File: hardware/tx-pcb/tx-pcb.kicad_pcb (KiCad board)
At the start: 4 copper layers, 70 x 79.1 mm, 61 parts, among them J1 Conn_To_J1, J2 Conn_To_J2, J3 BLIO, J4 Conn_01x05, J5 Conn_01x04, J6 PWRO, J7 Conn_01x02_Pin, SW1 BOOT0, SW2 RESET, SW3 BTN1, SW4 BTN2, SW5 BTN3, SW6 BTN4, SW7 BTN5, SW9 SW_SPDT, U2 STM32WB55CEUx, X1 Q22FA12800025, X2 ABS07-32.768KHZ-1-T

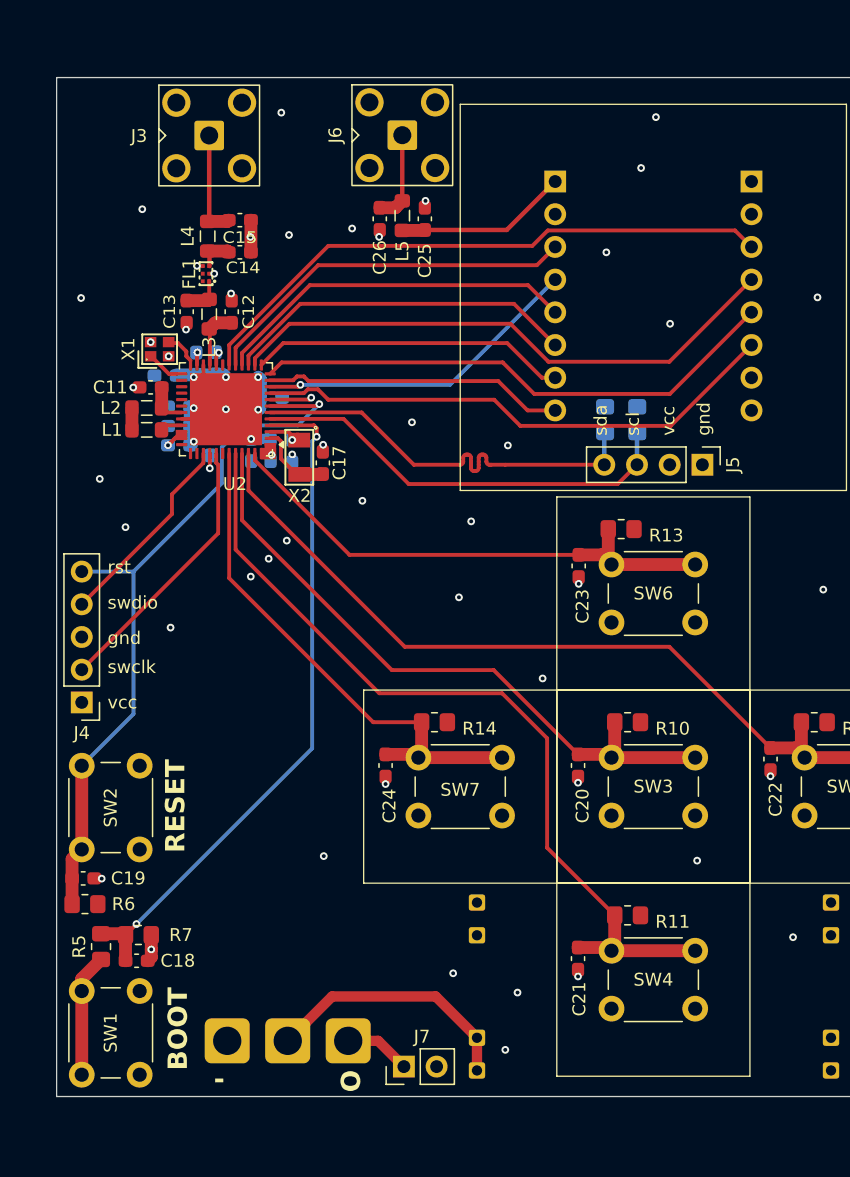
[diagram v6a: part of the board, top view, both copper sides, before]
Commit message: updated bluetooth output for MLPF chip and fixed ground layer issue
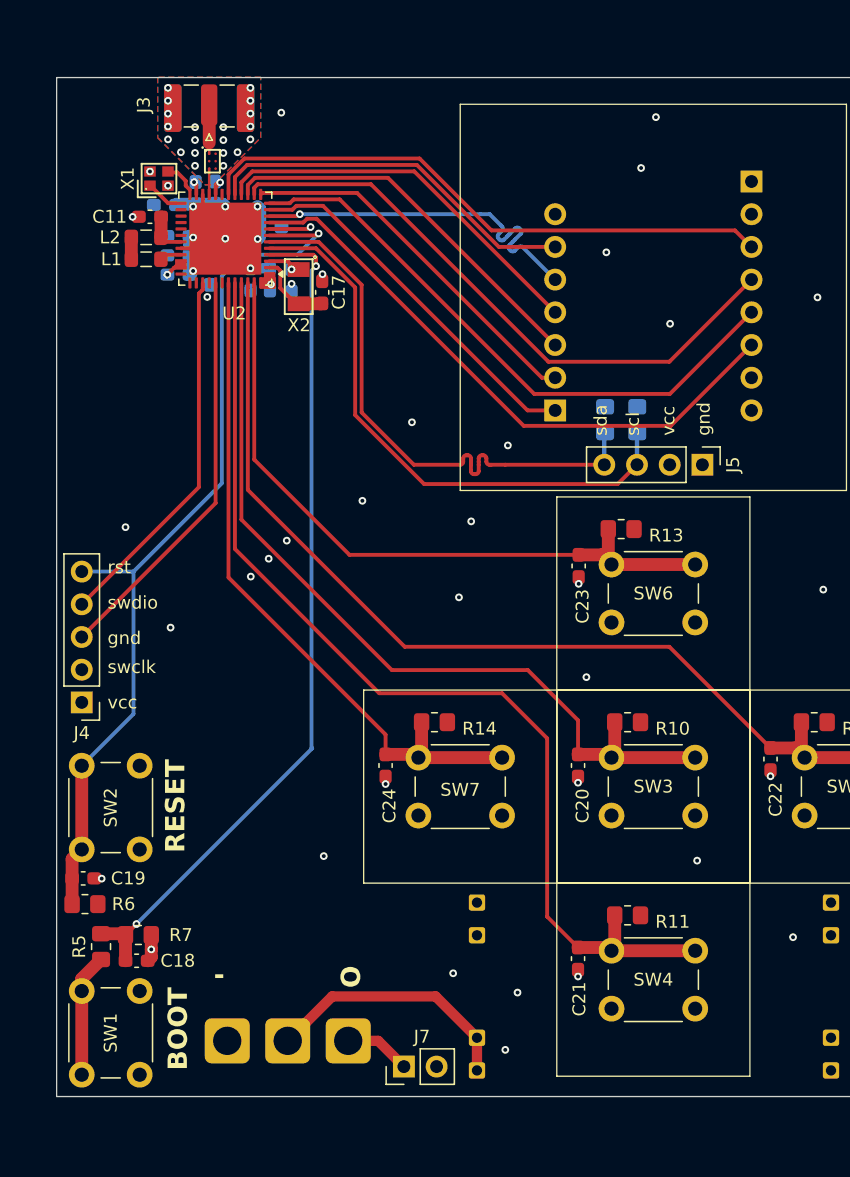
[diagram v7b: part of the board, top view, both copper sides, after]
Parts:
- removed C12: 0.8p, Capacitor_SMD:C_0603_1608Metric_Pad1.08x0.95mm_HandSolder
- removed C13: 0.3p, Capacitor_SMD:C_0603_1608Metric_Pad1.08x0.95mm_HandSolder
- removed C14, C15: NC, Capacitor_SMD:C_0603_1608Metric_Pad1.08x0.95mm_HandSolder
- removed C25, C26: C, Capacitor_SMD:C_0603_1608Metric_Pad1.08x0.95mm_HandSolder
- removed J6: PWRO, Connector_Coaxial:SMA_BAT_Wireless_BWSMA-KWE-Z001
- removed L3: 2.7n, Inductor_SMD:L_0805_2012Metric_Pad1.05x1.20mm_HandSolder
- removed L4: 0R, Inductor_SMD:L_0805_2012Metric_Pad1.05x1.20mm_HandSolder
- removed L5: L, Inductor_SMD:L_0805_2012Metric_Pad1.05x1.20mm_HandSolder
- FL1: value DLF162500LT-5028A1 -> MLPF-WB-01D3; footprint rf-pwr-tx-library:FILTER-SMD_6P-L1.6-W1.0-P0.50-BL -> easyeda2kicad:BGA-6_L1.6-W1.0-R3-C2-P0.50-TL
- J1: value Conn_To_J1 -> Conn_01x07; footprint Connector_PinHeader_2.54mm:PinHeader_1x08_P2.54mm_Vertical -> Connector_PinHeader_2.54mm:PinHeader_1x07_P2.54mm_Vertical
- J3: footprint Connector_Coaxial:SMA_BAT_Wireless_BWSMA-KWE-Z001 -> Connector_Coaxial:SMA_Samtec_SMA-J-P-H-ST-EM1_EdgeMount
- moved J1 17.8 mm to (173.4, 86.8), turned to 0 degrees
- moved L1 13.3 mm to (141.6, 75.0)
- moved X1 13.3 mm to (142.6, 68.8)
- moved C1 13.3 mm to (151.2, 72.5)
- moved C10 13.3 mm to (144.1, 73.2)
- moved C11 13.3 mm to (141.9, 71.7)
- moved C16 13.3 mm to (152.9, 76.7)
- moved C17 13.3 mm to (155.3, 77.6)
- moved C2 13.3 mm to (146.5, 76.2)
- moved C3 13.3 mm to (144.1, 76.2)
- moved C4 13.3 mm to (146.9, 69.9)
- moved C5 13.3 mm to (151.2, 76.6)
- moved C6 13.3 mm to (149.7, 76.6)
- moved C7 13.3 mm to (143.1, 70.8)
- moved C8 13.3 mm to (145.4, 69.9)
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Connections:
- J1 pad 1: Net-(J1-Pin_1) -> /SX1262_BUSY
- J1 pad 2: GND -> /SX1262_RST
- J1 pad 3: /SX1262_NSS -> /SPI_MISO
- J1 pad 4: /SPI_SCK -> /SPI_MOSI
- J1 pad 5: /SPI_MOSI -> /SPI_SCK
- J1 pad 6: /SPI_MISO -> /SX1262_NSS
- J1 pad 7: /SX1262_RST -> GND
- J3 pad 1: Net-(J3-In) -> Net-(FL1-OUT)
- J4 pad 2: /SWCLK -> GND
- J4 pad 3: GND -> /SWCLK
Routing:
- net /BTN2: track 65.7 -> 80.3 mm
- net /BTN1: track 51.2 -> 65.7 mm
- net Net-(J1-Pin_1): track 13.4 -> 0.00 mm
- net /BOOT0: track 53.2 -> 66.4 mm
- net /BTN4: track 40.9 -> 54.2 mm
- net /BTN3: track 64.0 -> 77.3 mm
- net /SWD_NSRT: track 57.2 -> 70.4 mm
- net /SWDIO: track 15.6 -> 28.9 mm
- net /BTN5: track 41.3 -> 53.7 mm
- net /I2C1_SDA: track 33.4 -> 45.0 mm
- net /I2C1_SCL: track 33.7 -> 45.1 mm
- net /SWCLK: track 21.3 -> 31.8 mm
- net Net-(J3-In): track 8.04 -> 0.00 mm
- net Net-(J6-In): track 7.07 -> 0.00 mm
- net /SX1262_DIO1: track 41.3 -> 46.8 mm
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- added copper zone on B.Cu, net GND
- added copper zone on F.Cu, net GND

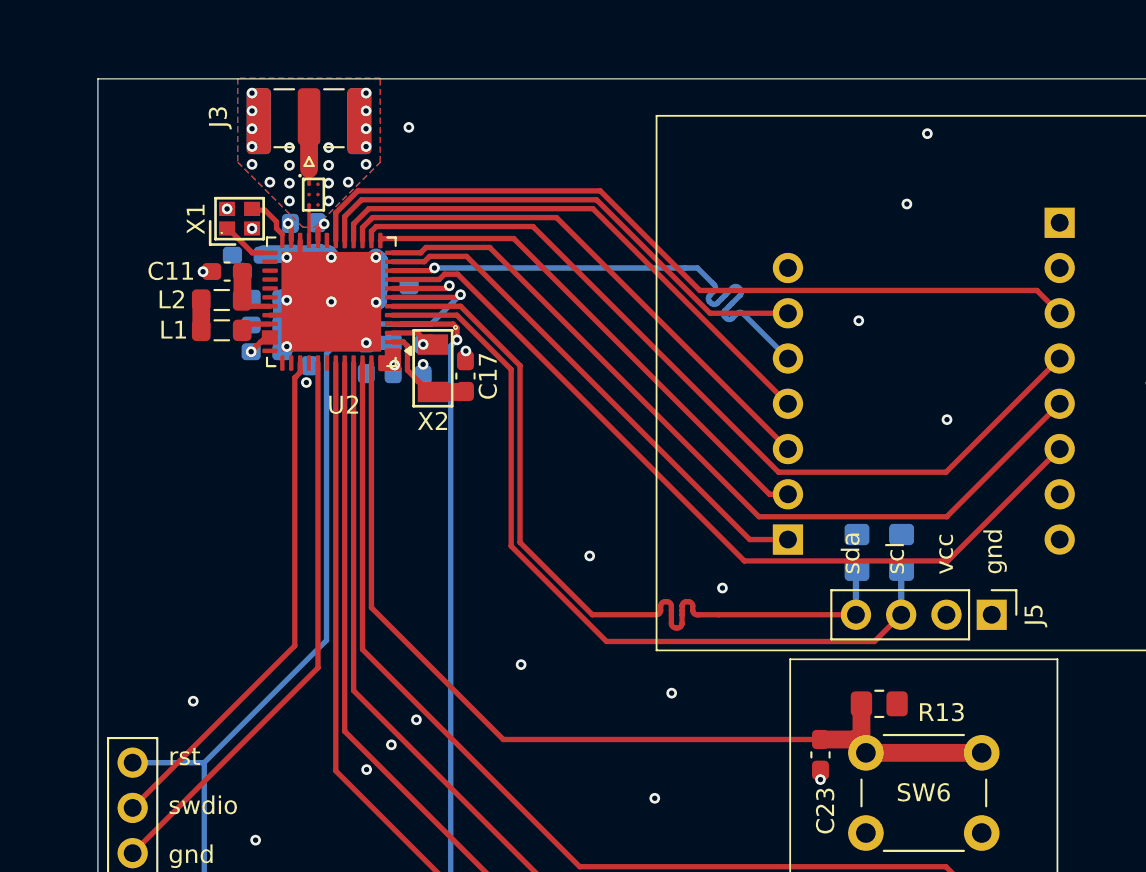
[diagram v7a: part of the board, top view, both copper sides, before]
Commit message: added UART to PCB, cleaned up wiring
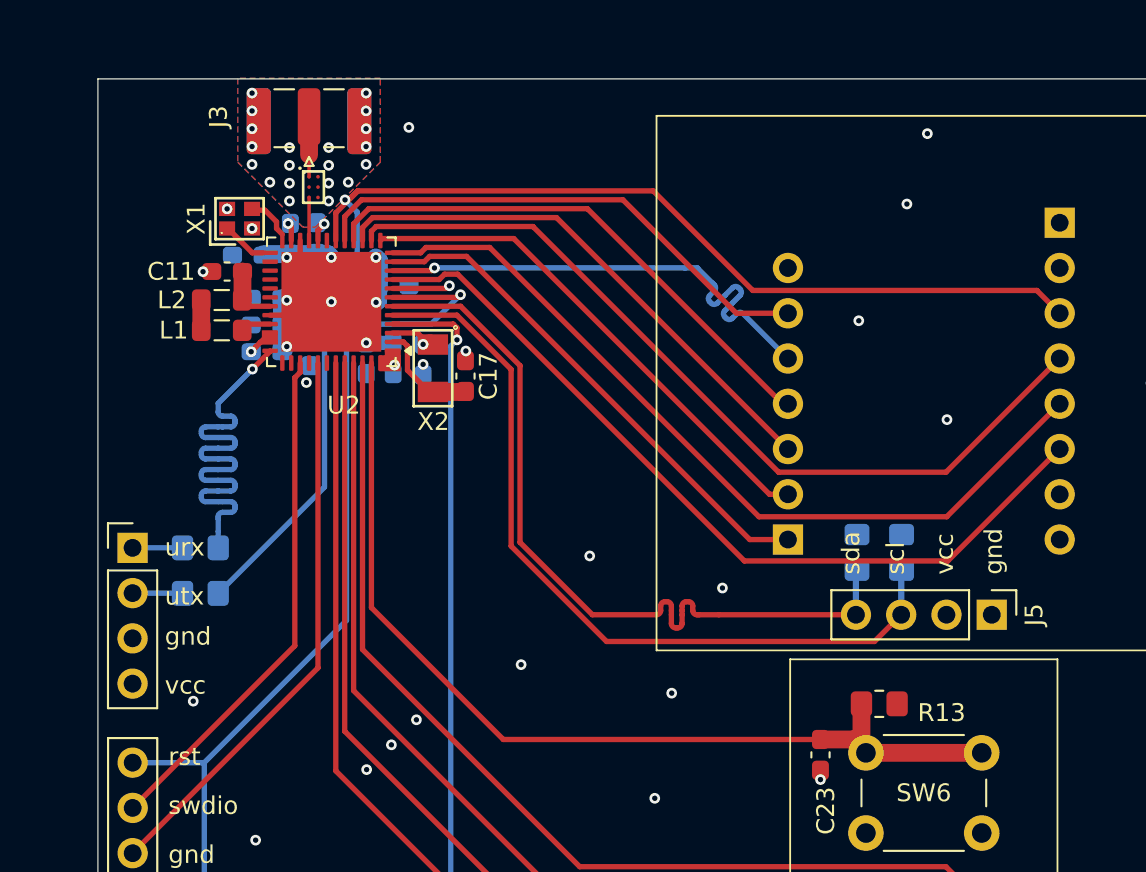
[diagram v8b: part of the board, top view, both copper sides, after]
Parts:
- added J6: Conn_01x04, Connector_PinHeader_2.54mm:PinHeader_1x04_P2.54mm_Vertical, F.Cu at (136.6, 87.2)
- added R1: 0, Resistor_SMD:R_0805_2012Metric_Pad1.20x1.40mm_HandSolder, B.Cu at (140.4, 87.2)
- added R2: 0, Resistor_SMD:R_0805_2012Metric_Pad1.20x1.40mm_HandSolder, B.Cu at (140.4, 89.8)
- J1: value Conn_01x07 -> Conn_To_J1
- moved FL1 0.42 mm to (146.8, 67.0)
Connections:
- U2 pad 36: unconnected-(U2-PA10-Pad36) -> Net-(U2-PA10)
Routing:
- net Net-(U2-PA10): track 0.00 -> 27.0 mm, vias 0 -> 1
- net /SX1262_RFSW#: track 45.5 -> 72.1 mm, vias 0 -> 1
- net /USART_TX: track 0.00 -> 2.81 mm
- net /USART_RX: track 0.00 -> 2.81 mm
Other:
- board text added: "urx"
- board text added: "utx"
